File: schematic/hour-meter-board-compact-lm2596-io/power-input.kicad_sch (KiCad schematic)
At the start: 25 parts, among them J101 VIN 9-30V, U101 LM2596S-ADJ

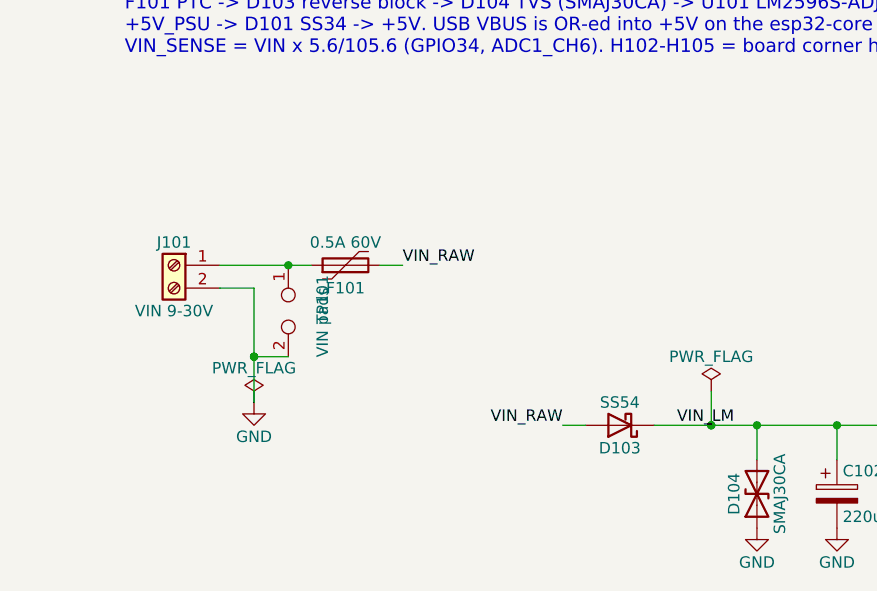
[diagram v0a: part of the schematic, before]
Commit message: fix(pcb): link the I/O board's TP101/TP102 solder pads to their nets
- TP101 (VIN) and TP102 (GND) replace the two-hole TP101: 1.5 mm pads on
  the back, above and below J101. They were placed by hand in the PCB
  editor, so they had no symbol link and no net and could not be routed
- they are now library footprints flipped to the bottom and linked to
  their symbols. A 0.5 mm B.Cu track joins J101 pin 1 to TP101, and TP102
  joins the GND pour solid (its thermal spokes were thinner than the
  pour's minimum)
- pours refilled, so the clearance and solder-mask errors are gone:
  DRC 0 errors, 0 unconnected, 0 parity
- tools-pcb.py: TP101/TP102 placed on the bottom side; `reuse` leaves out
  the LM2596 board's route to its two-hole TP101, which would cross TP102
- includes the board move and the KiCad 10 re-save of the sheets
- production: Gerbers and CPL regenerated, BOM unchanged
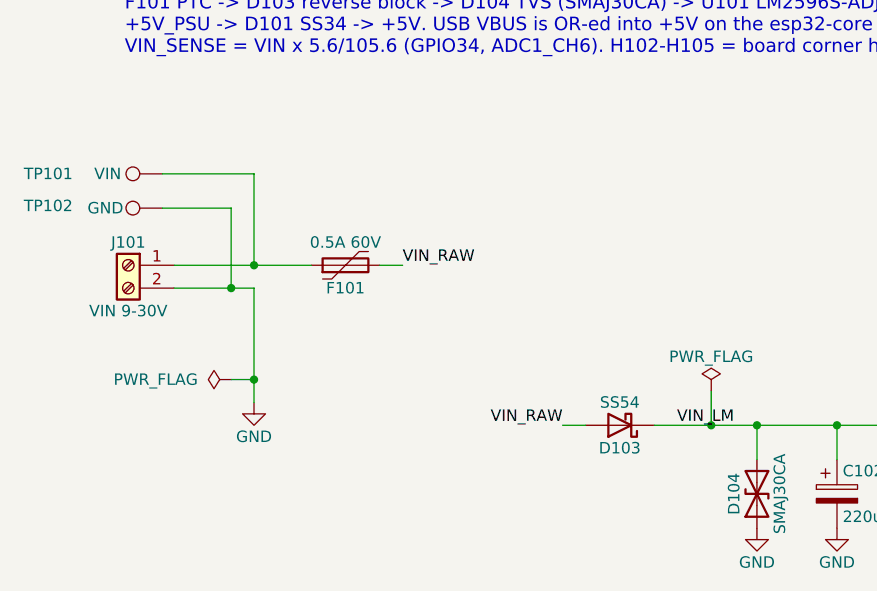
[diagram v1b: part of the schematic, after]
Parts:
- removed TP101: VIN pads, TestPoint:TestPoint_2Pads_Pitch5.08mm_Drill1.3mm, symbol Connector:TestPoint_2Pole
- added TP101: VIN, TestPoint:TestPoint_Pad_1.5x1.5mm, symbol Connector:TestPoint
- added TP102: GND, TestPoint:TestPoint_Pad_1.5x1.5mm, symbol Connector:TestPoint
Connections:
- net GND: now also TP102.1
- net at F101.1, J101.1 (Pin_1): now also TP101.1
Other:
- moved on the sheet: J101

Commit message: feat(pcb): enlarge the I/O board's VIN/GND solder pads to 3 mm
- TP101 (VIN) and TP102 (GND) use TestPoint_Pad_3.0x3.0mm, still on the
  bottom side above and below J101, for hand-soldering 18-22 AWG wire
- keep the GND track from J101 pin 2 to TP102 drawn in pcbnew
- tools-pcb.py: `reuse` leaves out both of the LM2596 board's routes from
  J101 to its two-hole TP101, following only branch-free track chains
- DRC 0 errors / 0 unconnected / 0 parity; Gerbers regenerated, BOM and
  CPL unchanged
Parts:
- TP101, TP102: footprint TestPoint:TestPoint_Pad_1.5x1.5mm -> TestPoint:TestPoint_Pad_3.0x3.0mm
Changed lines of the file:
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@@
 			)
 		)
-		(property "Footprint" "TestPoint:TestPoint_Pad_1.5x1.5mm"
+		(property "Footprint" "TestPoint:TestPoint_Pad_3.0x3.0mm"
 			(at 29.21 48.26 0)
 			(hide yes)
@@
 			)
 		)
-		(property "Footprint" "TestPoint:TestPoint_Pad_1.5x1.5mm"
+		(property "Footprint" "TestPoint:TestPoint_Pad_3.0x3.0mm"
 			(at 29.21 44.45 0)
 			(hide yes)
